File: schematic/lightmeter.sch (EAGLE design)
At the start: 71 parts, among them J1 CONNECTEDJUMPER, J2 CONNECTEDJUMPER, J3 CONNECTEDJUMPER, J4 CONNECTEDJUMPER, J5 CONNECTEDJUMPER, J6 CONNECTEDJUMPER, Q1 NCHANNELMOSFET, Q2 NCHANNELMOSFET, Q3 PCHANNELMOSFET

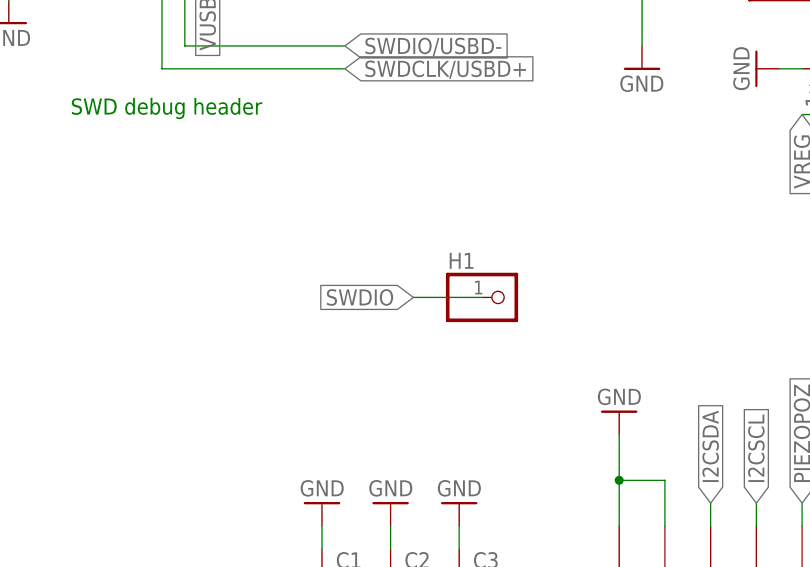
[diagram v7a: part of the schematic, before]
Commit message: Delete unneeded SWDIO header.
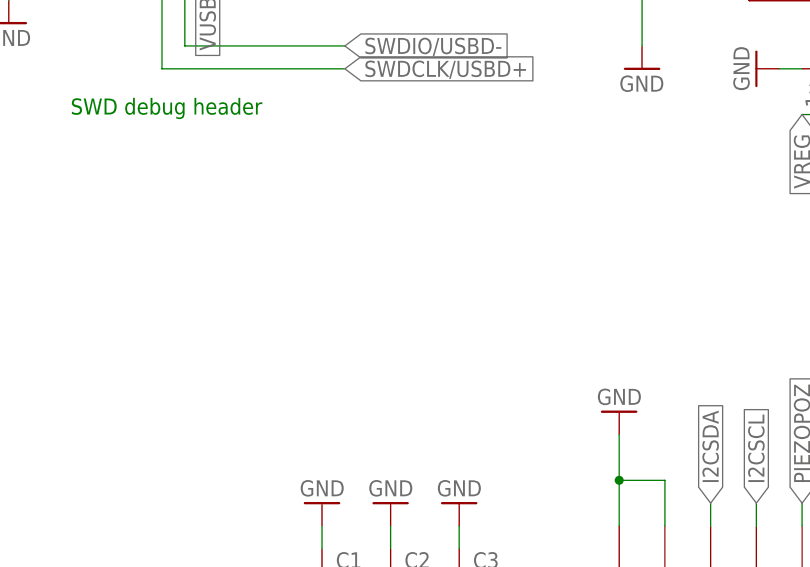
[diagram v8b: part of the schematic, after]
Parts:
- removed H1: (no value), pinhead:PINHD-1X1
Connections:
- removed net SWDIO: H1.1
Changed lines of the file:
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@@
 <part name="J1" library="lightmeter" deviceset="CONNECTEDJUMPER" device=""/>
 <part name="J2" library="lightmeter" deviceset="CONNECTEDJUMPER" device=""/>
-<part name="H1" library="pinhead" deviceset="PINHD-1X1" device=""/>
 <part name="J3" library="lightmeter" deviceset="CONNECTEDJUMPER" device=""/>
 <part name="J4" library="lightmeter" deviceset="CONNECTEDJUMPER" device=""/>
@@
 <instance part="J1" gate="G$1" x="190.5" y="-106.68"/>
 <instance part="J2" gate="G$1" x="190.5" y="-132.08"/>
-<instance part="H1" gate="G$1" x="-63.5" y="48.26"/>
 <instance part="J3" gate="G$1" x="38.1" y="-2.032" rot="R90"/>
 <instance part="J4" gate="G$1" x="142.24" y="-106.68"/>
@@
 </segment>
 </net>
-<net name="SWDIO" class="0">
-<segment>
-<pinref part="H1" gate="G$1" pin="1"/>
-<wire x1="-66.04" y1="48.26" x2="-73.66" y2="48.26" width="0.1524" layer="91"/>
-<label x="-73.66" y="48.26" size="1.778" layer="95" rot="R180" xref="yes"/>
-</segment>
-</net>
